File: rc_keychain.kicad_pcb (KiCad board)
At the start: 4 copper layers, 100 x 80 mm, 211 parts, among them J1 U.FL-R-SMT-1(10), J2 TYPE-C 16PIN 2MD(073), J3 Touch_Surface_Top, J4 Touch_Surface_Bottom, J5 5034801200, Q1 2N7002, SW1 TS35CA, U1 SF32LB525UC6, U10 LIS2DW12TR, U11 AP3602AKTR-G1, U12 SN74AUP1G17, U13 ST25R3916B-AQET, U2 MKDV1GCL-ABA, U3 TPS25200DRVT, U4 USBLC6-2P6, U5 USBLC6-2P6, U6 CAP1208-1-A4-TR, U7 CAP1208-1-A4-TR, U8 DRV2603RUNT, U9 TPS61040DBV, Y1 48MHz, Y2 32.768khz, Y3 27.12MHz

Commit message: fixups before manufacturing pt1
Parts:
- U10: value LIS2DW12TR -> LIS3DH; footprint LIS2DW12TR:LGA-12_L2.0-W2.0-P0.50-BL -> Package_LGA:LGA-16_3x3mm_P0.5mm_LayoutBorder3x5y
- moved JP15 2.61 mm to (126.5, 80.8)
- moved JP14 2.59 mm to (126.5, 83.4)
- moved C33 1.04 mm to (129.4, 80.0)
- moved C34 0.76 mm to (132.0, 79.1), turned to 90 degrees
- moved C35 0.70 mm to (131.0, 79.1), turned to 90 degrees
- moved U10 0.60 mm to (131.7, 82.0)
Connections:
- U10 pad 1: Net-(JP14-B) -> /interface/ACC_3V3_IN
- U10 pad 10: /interface/ACC_3V3_IN -> GND
- U10 pad 11: unconnected-(U10-INT2-Pad11) -> Net-(JP17-A)
- U10 pad 12: Net-(JP17-A) -> GND
- U10 pad 5: unconnected-(U10-NC-Pad5) -> GND
- U10 pad 6: GND -> Net-(JP14-B)
- U10 pad 7: GND -> unconnected-(U10-SDO-Pad7)
- U10 pad 8: GND -> /interface/ACC_3V3_IN
- U10 pad 9: /interface/ACC_3V3_IN -> unconnected-(U10-INT2-Pad9)
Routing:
- net Net-(JP17-A): track 5.57 -> 11.6 mm
- net /interface/ACC_3V3_IN: track 6.16 -> 8.99 mm
- net Net-(JP15-B): track 5.41 -> 4.00 mm
- net SDA: track 83.8 -> 85.0 mm
- net SCL: track 80.7 -> 81.8 mm
- net GND: track 110.8 -> 110.9 mm, vias 120 -> 123
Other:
- outline, holes or cut-outs redrawn

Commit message: fixups before manufacturing pt2
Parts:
- removed R1: 7.5k, Resistor_SMD:R_0603_1608Metric
- TP18: value SD_CLK -> FLASH_CLK
- TP19: value SD_CLK -> FLASH_CS
- TP20: value SD_DAT0 -> FLASH_DIO0
- TP21: value SD_DAT1 -> FLASH_DIO1
- TP22: value SD_DAT2 -> FLASH_DIO2
- TP23: value SD_DAT3 -> FLASH_DIO3
- U2: value MKDV1GCL-ABA -> GD25Q256EWIGR; footprint MKDV1GCL-ABA:LGA-8_L6.0-W8.0-P1.27-TL -> GD25Q256EWIGR:WSON-8_L6.0-W5.0-P1.27-TL-EP
- moved TP19 13.2 mm to (119.6, 111.8)
- moved TP23 12.0 mm to (129.8, 113.0)
- moved TP21 9.92 mm to (122.4, 109.6)
- moved TP22 8.06 mm to (124.5, 109.5)
- moved TP18 5.64 mm to (126.7, 109.6)
- moved TP20 2.06 mm to (130.5, 115.1)
- moved C5 1.45 mm to (128.9, 111.1)
- moved TP26 1.21 mm to (130.1, 108.9)
- moved U2 0.33 mm to (124.8, 113.4)
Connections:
- TP18 pad 1: SD_CLK -> FLASH_CLK
- TP19 pad 1: SD_CMD -> FLASH_CS
- TP20 pad 1: SD_DAT0 -> FLASH_DIO0
- TP21 pad 1: SD_DAT1 -> FLASH_DIO1
- TP22 pad 1: SD_DAT2 -> FLASH_DIO2
- TP23 pad 1: SD_DAT3 -> FLASH_DIO3
- U1 pad 28: SD_DAT1 -> FLASH_DIO3
- U1 pad 29: SD_DAT0 -> FLASH_CLK
- U1 pad 30: SD_CMD -> FLASH_DIO0
- U1 pad 31: SD_CLK -> FLASH_DIO2
- U1 pad 32: SD_DAT3 -> FLASH_DIO1
- U1 pad 33: SD_DAT2 -> FLASH_CS
- U2 pad 1: SD_DAT2 -> FLASH_CS
- U2 pad 2: SD_DAT3 -> FLASH_DIO1
- U2 pad 3: SD_CLK -> FLASH_DIO2
- U2 pad 5: SD_CMD -> FLASH_DIO0
- U2 pad 6: SD_DAT0 -> FLASH_CLK
- U2 pad 7: SD_DAT1 -> FLASH_DIO3
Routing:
- net SD_DAT3: track 22.0 -> 0.00 mm
- net SD_DAT1: track 20.3 -> 0.00 mm, vias 2 -> 0
- net FLASH_CLK: track 0.00 -> 18.0 mm
- net SD_DAT0: track 17.7 -> 0.00 mm, vias 2 -> 0
- net FLASH_DIO3: track 0.00 -> 16.5 mm
- net SD_CLK: track 16.2 -> 0.00 mm
- net FLASH_DIO0: track 0.00 -> 15.8 mm, vias 0 -> 2
- net SD_CMD: track 15.2 -> 0.00 mm
- net FLASH_DIO2: track 0.00 -> 14.8 mm
- net FLASH_CS: track 0.00 -> 14.1 mm
- net SD_DAT2: track 13.9 -> 0.00 mm
- net FLASH_DIO1: track 0.00 -> 13.8 mm
- net +3V3_G1: track 14.0 -> 12.4 mm, vias 4 -> 3
- net GND: track 110.9 -> 110.7 mm, vias 123 -> 124

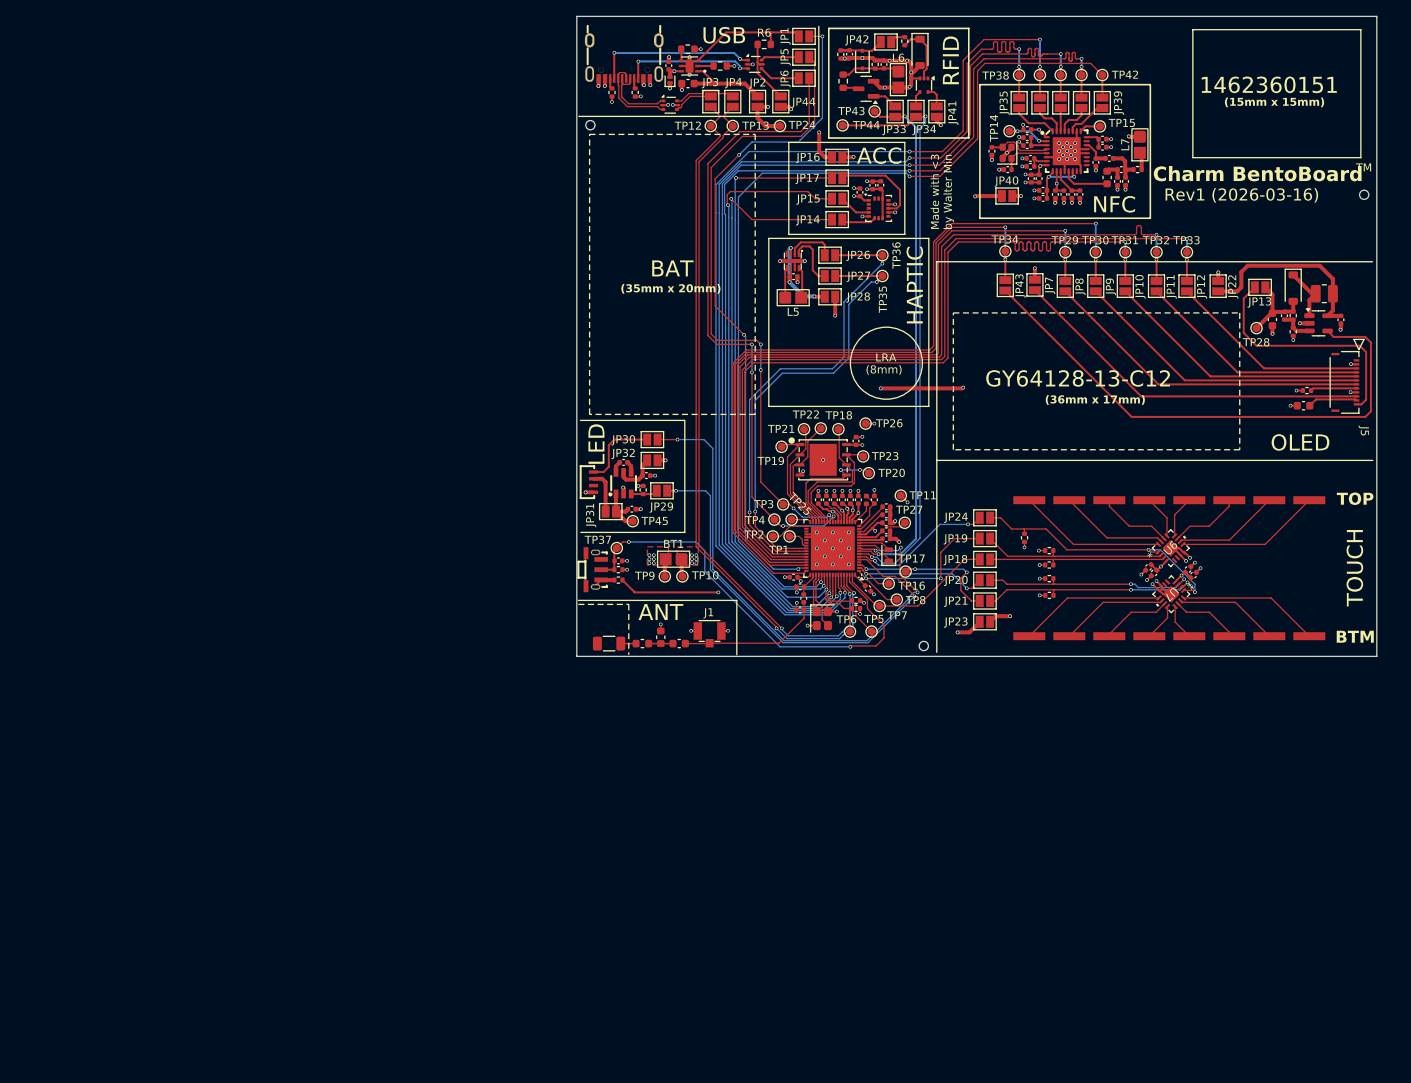
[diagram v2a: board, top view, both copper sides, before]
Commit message: revise some decoupling caps to be 0201
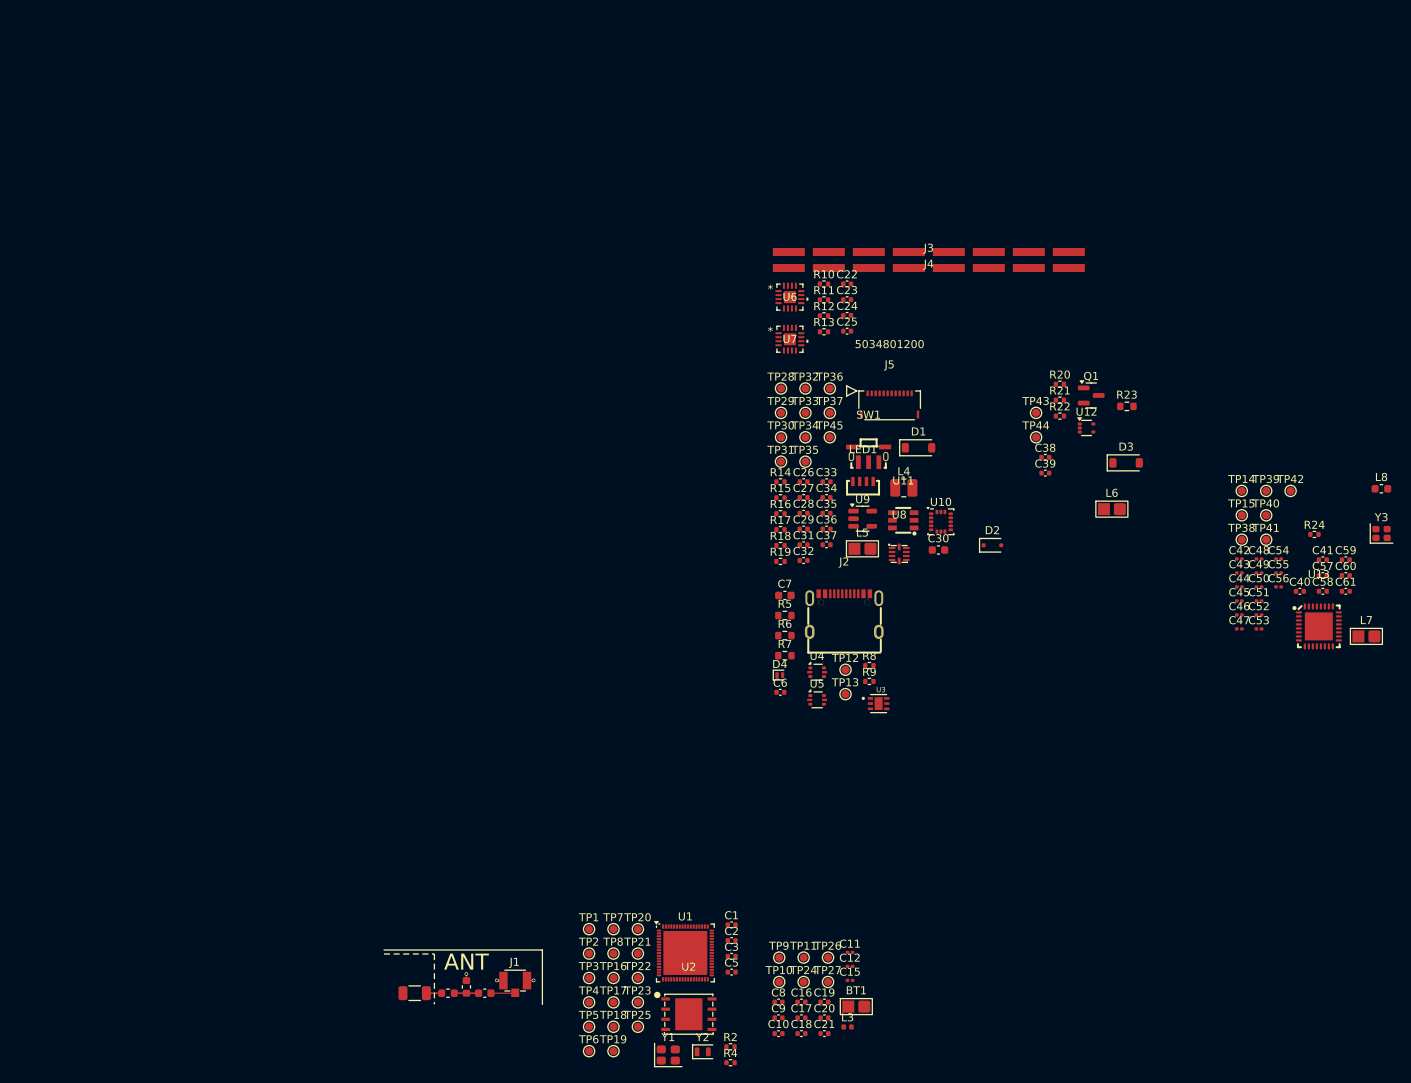
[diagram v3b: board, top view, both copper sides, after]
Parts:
- removed C13, C14: 4.7uF, Capacitor_SMD:C_0402_1005Metric
- removed JP1: USB_OVP_FAULT, Jumper:SolderJumper-2_P1.3mm_Open_Pad1.0x1.5mm
- removed JP10: OLED_DC, Jumper:SolderJumper-2_P1.3mm_Open_Pad1.0x1.5mm
- removed JP11: OLED_CLK, Jumper:SolderJumper-2_P1.3mm_Open_Pad1.0x1.5mm
- removed JP12: OLED_DAT, Jumper:SolderJumper-2_P1.3mm_Open_Pad1.0x1.5mm
- removed JP13: OLED_9V, Jumper:SolderJumper-2_P1.3mm_Open_Pad1.0x1.5mm
- removed JP14: ACC_SCL, Jumper:SolderJumper-2_P1.3mm_Open_Pad1.0x1.5mm
- removed JP15: ACC_SDA, Jumper:SolderJumper-2_P1.3mm_Open_Pad1.0x1.5mm
- removed JP16: ACC_3V3, Jumper:SolderJumper-2_P1.3mm_Open_Pad1.0x1.5mm
- removed JP17: ACC_INT, Jumper:SolderJumper-2_P1.3mm_Open_Pad1.0x1.5mm
- removed JP18: TOUCH_SCL_T1, Jumper:SolderJumper-2_P1.3mm_Open_Pad1.0x1.5mm
- removed JP19: TOUCH_SDA_T1, Jumper:SolderJumper-2_P1.3mm_Open_Pad1.0x1.5mm
- removed JP2: USB_VBUS, Jumper:SolderJumper-2_P1.3mm_Open_Pad1.0x1.5mm
- removed JP20: TOUCH_SCL_T2, Jumper:SolderJumper-2_P1.3mm_Open_Pad1.0x1.5mm
- removed JP21: TOUCH_SDA_T2, Jumper:SolderJumper-2_P1.3mm_Open_Pad1.0x1.5mm
- removed JP22: OLED_VBAT, Jumper:SolderJumper-2_P1.3mm_Open_Pad1.0x1.5mm
- removed JP23: TOUCH_3V3_G2, Jumper:SolderJumper-2_P1.3mm_Open_Pad1.0x1.5mm
- removed JP24: TOUCH_INT, Jumper:SolderJumper-2_P1.3mm_Open_Pad1.0x1.5mm
- removed JP26: HAPTIC_PWM, Jumper:SolderJumper-2_P1.3mm_Open_Pad1.0x1.5mm
- removed JP27: HAPTIC_EN, Jumper:SolderJumper-2_P1.3mm_Open_Pad1.0x1.5mm
- removed JP28: HAPTIC_VBAT, Jumper:SolderJumper-2_P1.3mm_Open_Pad1.0x1.5mm
- removed JP29: LED_EN, Jumper:SolderJumper-2_P1.3mm_Open_Pad1.0x1.5mm
- removed JP3: USB_DP, Jumper:SolderJumper-2_P1.3mm_Open_Pad1.0x1.5mm
- removed JP30: LED_DAT, Jumper:SolderJumper-2_P1.3mm_Open_Pad1.0x1.5mm
- removed JP31: LED_5V, Jumper:SolderJumper-2_P1.3mm_Open_Pad1.0x1.5mm
- removed JP32: LED_VBAT, Jumper:SolderJumper-2_P1.3mm_Open_Pad1.0x1.5mm
- removed JP33: RFID_DAT, Jumper:SolderJumper-2_P1.3mm_Open_Pad1.0x1.5mm
- removed JP34: RFID_WAKE, Jumper:SolderJumper-2_P1.3mm_Open_Pad1.0x1.5mm
- removed JP35: NFC_DI, Jumper:SolderJumper-2_P1.3mm_Open_Pad1.0x1.5mm
- removed JP36: NFC_DO, Jumper:SolderJumper-2_P1.3mm_Open_Pad1.0x1.5mm
- removed JP37: NFC_CLK, Jumper:SolderJumper-2_P1.3mm_Open_Pad1.0x1.5mm
- removed JP38: NFC_CS, Jumper:SolderJumper-2_P1.3mm_Open_Pad1.0x1.5mm
- removed JP39: NFC_INT, Jumper:SolderJumper-2_P1.3mm_Open_Pad1.0x1.5mm
- removed JP4: USB_DN, Jumper:SolderJumper-2_P1.3mm_Open_Pad1.0x1.5mm
- removed JP40: NFC_3V3, Jumper:SolderJumper-2_P1.3mm_Open_Pad1.0x1.5mm
- removed JP41: RFID_3V3, Jumper:SolderJumper-2_P1.3mm_Open_Pad1.0x1.5mm
- removed JP42: RFID_WAKE_RAW, Jumper:SolderJumper-2_P1.3mm_Open_Pad1.0x1.5mm
- removed JP43: OLED_EN, Jumper:SolderJumper-2_P1.3mm_Open_Pad1.0x1.5mm
- removed JP44: USB_3V3, Jumper:SolderJumper-2_P1.3mm_Open_Pad1.0x1.5mm
- removed JP5: USB_DBG_A, Jumper:SolderJumper-2_P1.3mm_Open_Pad1.0x1.5mm
- removed JP6: USB_DBG_B, Jumper:SolderJumper-2_P1.3mm_Open_Pad1.0x1.5mm
- removed JP7: OLED_3V3_G2, Jumper:SolderJumper-2_P1.3mm_Open_Pad1.0x1.5mm
- removed JP8: OLED_CS, Jumper:SolderJumper-2_P1.3mm_Open_Pad1.0x1.5mm
- removed JP9: OLED_RST, Jumper:SolderJumper-2_P1.3mm_Open_Pad1.0x1.5mm
- removed R3: 100k, Resistor_SMD:R_0402_1005Metric
- C11, C12, C15, C42, C43, C44, C45, C46, C47, C48, C49, C50, C51, C52, C53, C54, C55, C56: footprint Capacitor_SMD:C_0402_1005Metric -> Capacitor_SMD:C_0201_0603Metric
- C28: footprint Capacitor_SMD:C_0603_1608Metric -> Capacitor_SMD:C_0402_1005Metric
- moved TP24 107.0 mm to (122.4, 178.7)
- moved U3 83.1 mm to (131.7, 143.9), turned to 0 degrees
- moved R9 80.3 mm to (130.6, 141.1), turned to 0 degrees
- moved U5 79.8 mm to (124.0, 143.4)
- moved TP18 79.8 mm to (98.6, 184.3)
- moved C6 79.6 mm to (119.4, 142.5), turned to 0 degrees
- moved TP19 78.4 mm to (98.6, 187.3)
- moved R8 77.4 mm to (130.6, 139.1), turned to 0 degrees
- moved D4 75.6 mm to (119.4, 140.3), turned to 0 degrees
- moved J2 74.4 mm to (127.4, 132.6), turned to 0 degrees
- moved R7 74.2 mm to (120.0, 137.9)
- moved R6 73.9 mm to (120.0, 135.4)
- moved TP23 73.8 mm to (101.6, 181.2)
- moved U4 73.2 mm to (124.0, 140.0)
- moved TP13 72.4 mm to (127.6, 142.7)
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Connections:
- C22 pad 1: /touch/+3V3_G2_IN -> +3V3_G2
- C23 pad 1: /touch/+3V3_G2_IN -> +3V3_G2
- C24 pad 1: /touch/+3V3_G2_IN -> +3V3_G2
- C25 pad 1: /touch/+3V3_G2_IN -> +3V3_G2
- C26 pad 1: /interface/HAPTIC_VBAT_IN -> VBAT
- C27 pad 1: Net-(JP22-B) -> VBAT
- C29 pad 1: Net-(D1-A) -> +9V
- C30 pad 1: Net-(D1-A) -> +9V
- C32 pad 1: Net-(JP32-B) -> VBAT
- C33 pad 1: /interface/ACC_3V3_IN -> +3V3
- C34 pad 1: /interface/ACC_3V3_IN -> +3V3
- C35 pad 1: /interface/ACC_3V3_IN -> +3V3
- C37 pad 1: Net-(JP31-A) -> +5V
- C38 pad 1: Net-(D2-K) -> Net-(D2-A)
- C39 pad 2: Net-(D2-A) -> Net-(D2-K)
- C44 pad 1: /rf/NFC_3V3_IN -> +3V3
- C51 pad 1: /rf/NFC_3V3_IN -> +3V3
- C52 pad 1: /rf/NFC_3V3_IN -> +3V3
- C53 pad 1: /rf/NFC_3V3_IN -> +3V3
- C54 pad 1: /rf/NFC_3V3_IN -> +3V3
- C7 pad 1: Net-(JP2-A) -> VBUS
- D1 pad 1: Net-(D1-K) -> +9V
- D4 pad 1: GND -> /usb/VBUS_RAW
- D4 pad 2: /usb/VBUS_RAW -> GND
- J5 pad 10: /interface/+3V3_G2_IN -> +3V3_G2
- J5 pad 3: /interface/OLED_DAT_IN -> OLED_DAT
- J5 pad 4: /interface/OLED_CLK_IN -> OLED_CLK
- J5 pad 5: /interface/OLED_DC_IN -> OLED_DC
- J5 pad 6: /interface/OLED_RST_IN -> OLED_RST
- J5 pad 7: /interface/OLED_CS_IN -> OLED_CS
- L4 pad 1: Net-(JP22-B) -> VBAT
- L4 pad 2: Net-(D1-K) -> Net-(D1-A)
- L6 pad 2: Net-(D2-K) -> Net-(D2-A)
- LED1 pad 4: /interface/LED_DAT_IN -> LED_DAT
- Q1 pad 1: /rf/RFID_DAT_IN -> RFID_DAT
- R10 pad 1: /touch/+3V3_G2_IN -> +3V3_G2
- R10 pad 2: Net-(JP19-B) -> SDA_T1
- R11 pad 1: /touch/+3V3_G2_IN -> +3V3_G2
- R11 pad 2: Net-(JP21-B) -> SDA_T2
- R12 pad 1: /touch/+3V3_G2_IN -> +3V3_G2
- R12 pad 2: Net-(JP18-B) -> SCL_T1
- R13 pad 1: /touch/+3V3_G2_IN -> +3V3_G2
- R13 pad 2: Net-(JP20-B) -> SCL_T2
- R16 pad 1: Net-(D1-A) -> +9V
- R19 pad 1: /interface/LED_EN_IN -> LED_EN
- R20 pad 1: Net-(D2-K) -> Net-(D2-A)
- R21 pad 1: Net-(JP42-B) -> Net-(D2-K)
- R22 pad 1: Net-(D2-A) -> Net-(D2-K)
- R23 pad 1: Net-(D2-K) -> Net-(D2-A)
- R6 pad 1: /usb/USB_3V3_IN -> +3V3
- R6 pad 2: Net-(JP1-A) -> OVP_FAULT
- TP28 pad 1: Net-(D1-A) -> +9V
- TP45 pad 1: Net-(JP31-A) -> +5V
- U10 pad 1: /interface/ACC_3V3_IN -> +3V3
- U10 pad 11: Net-(JP17-A) -> ACC_INT
- U10 pad 14: /interface/ACC_3V3_IN -> +3V3
- U10 pad 4: Net-(JP15-B) -> SCL
- U10 pad 6: Net-(JP14-B) -> SDA
- U10 pad 7: unconnected-(U10-SDO-Pad7) -> GND
- U11 pad 1: Net-(JP31-A) -> +5V
- U11 pad 3: /interface/LED_EN_IN -> LED_EN
- U11 pad 5: Net-(JP32-B) -> VBAT
- U12 pad 4: /rf/RFID_WAKE_IN -> RFID_WAKE
- U12 pad 5: /rf/RFID_3V3_IN -> +3V3
- U13 pad 1: /rf/NFC_3V3_IN -> +3V3
- U13 pad 10: /rf/NFC_3V3_IN -> +3V3
- U13 pad 27: /rf/NFC_INT_IN -> NFC_INT
- U13 pad 29: /rf/NFC_CS_IN -> NFC_CS
- U13 pad 30: /rf/NFC_CLK_IN -> NFC_CLK
- U13 pad 31: /rf/NFC_DO_IN -> NFC_DO
- U13 pad 32: /rf/NFC_DI_IN -> NFC_DI
- U13 pad 8: /rf/NFC_3V3_IN -> +3V3
- U3 pad 1: Net-(JP2-A) -> VBUS
- U3 pad 3: Net-(JP1-A) -> OVP_FAULT
- U4 pad 4: /usb/USB_PROT_DP -> USB_DP
- U4 pad 6: /usb/USB_PROT_DN -> USB_DN
- U5 pad 4: Net-(JP6-A) -> DBG_B
- U5 pad 6: Net-(JP5-A) -> DBG_A
- U6 pad 1: /touch/TOUCH_INT_IN -> TOUCH_INT
- U6 pad 2: Net-(JP19-B) -> SDA_T1
- U6 pad 3: Net-(JP18-B) -> SCL_T1
- U6 pad 4: /touch/+3V3_G2_IN -> +3V3_G2
- U7 pad 1: /touch/TOUCH_INT_IN -> TOUCH_INT
- U7 pad 2: Net-(JP21-B) -> SDA_T2
- U7 pad 3: Net-(JP20-B) -> SCL_T2
- U7 pad 4: /touch/+3V3_G2_IN -> +3V3_G2
- U8 pad 1: Net-(JP27-B) -> HAPTIC_EN
- U8 pad 2: Net-(JP26-B) -> HAPTIC_PWM
- U8 pad 3: /interface/HAPTIC_VBAT_IN -> VBAT
- U8 pad 7: /interface/HAPTIC_VBAT_IN -> VBAT
- U9 pad 1: Net-(D1-K) -> Net-(D1-A)
- U9 pad 4: /interface/OLED_EN_IN -> OLED_EN
- U9 pad 5: Net-(JP22-B) -> VBAT
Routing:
- net NFC_DO: track 129.2 -> 0.00 mm, vias 4 -> 0
- net NFC_CS: track 129.2 -> 0.00 mm, vias 4 -> 0
- net NFC_CLK: track 129.2 -> 0.00 mm, vias 4 -> 0
- net NFC_DI: track 129.1 -> 0.00 mm, vias 4 -> 0
- net NFC_INT: track 118.0 -> 0.00 mm, vias 2 -> 0
- net GND: track 110.7 -> 2.50 mm, vias 124 -> 3
- net OLED_DAT: track 105.5 -> 0.00 mm, vias 2 -> 0
- net OLED_CLK: track 105.5 -> 0.00 mm, vias 2 -> 0
- net OLED_DC: track 105.4 -> 0.00 mm, vias 2 -> 0
- net OLED_RST: track 100.9 -> 0.00 mm, vias 2 -> 0
- net OLED_CS: track 94.0 -> 0.00 mm, vias 2 -> 0
- net USB_DP: track 89.8 -> 0.00 mm, vias 2 -> 0
- net USB_DN: track 88.3 -> 0.00 mm, vias 2 -> 0
- net OLED_EN: track 87.8 -> 0.00 mm, vias 2 -> 0
- net SDA: track 85.0 -> 0.00 mm, vias 2 -> 0
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- added copper zone on In2.Cu, net (none)
- removed copper zone on In2.Cu, net /interface/HAPTIC_VBAT_IN
- removed copper zone on In2.Cu, net /rf/NFC_3V3_IN
- removed copper zone on In2.Cu, net /touch/+3V3_G2_IN
- removed copper zone on F.Cu, net GND
- removed copper zone on F.Cu, net VBAT
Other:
- board outline removed
- board text removed: "(15mm x 15mm)"
- board text removed: "(35mm x 20mm)"
- board text removed: "(36mm x 17mm)"
- board text removed: "(8mm)"
- board text removed: "1462360151"
- board text removed: "ACC"
- board text removed: "BAT"
- board text removed: "BTM"
- board text removed: "Charm BentoBoard"
- board text removed: "GY64128-13-C12"
- board text removed: "HAPTIC"
- board text removed: "LED"
- board text removed: "LRA"
- board text removed: "Made with <3 by Walter Min"
- board text removed: "NFC"
- board text removed: "OLED"
- board text removed: "RFID"
- board text removed: "Rev1 (2026-03-16)"
- board text removed: "TM"
- board text removed: "TOP"
- board text removed: "TOUCH"
- board text removed: "USB"

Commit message: layout progress
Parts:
- removed J1: U.FL-R-SMT-1(10), U.FL-R-SMT-1_10_:HRS_U.FL-R-SMT-1_10_
- removed TP18: FLASH_CLK, TestPoint:TestPoint_Pad_D1.0mm
- removed TP19: FLASH_CS, TestPoint:TestPoint_Pad_D1.0mm
- removed TP20: FLASH_DIO0, TestPoint:TestPoint_Pad_D1.0mm
- removed TP21: FLASH_DIO1, TestPoint:TestPoint_Pad_D1.0mm
- removed TP22: FLASH_DIO2, TestPoint:TestPoint_Pad_D1.0mm
- removed TP23: FLASH_DIO3, TestPoint:TestPoint_Pad_D1.0mm
- removed TP29: OLED_CS, TestPoint:TestPoint_Pad_D1.0mm
- removed TP30: OLED_RST, TestPoint:TestPoint_Pad_D1.0mm
- removed TP31: OLED_DC, TestPoint:TestPoint_Pad_D1.0mm
- removed TP32: OLED_CLK, TestPoint:TestPoint_Pad_D1.0mm
- removed TP33: OLED_DAT, TestPoint:TestPoint_Pad_D1.0mm
- removed TP34: OLED_EN, TestPoint:TestPoint_Pad_D1.0mm
- removed TP35: HAPTIC_EN, TestPoint:TestPoint_Pad_D1.0mm
- removed TP36: HAPTIC_PWM, TestPoint:TestPoint_Pad_D1.0mm
- removed TP38: NFC_DI, TestPoint:TestPoint_Pad_D1.0mm
- removed TP39: NFC_DO, TestPoint:TestPoint_Pad_D1.0mm
- removed TP40: NFC_CLK, TestPoint:TestPoint_Pad_D1.0mm
- removed TP41: NFC_CS, TestPoint:TestPoint_Pad_D1.0mm
- removed TP42: NFC_INT, TestPoint:TestPoint_Pad_D1.0mm
- removed TP43: RFID_DAT, TestPoint:TestPoint_Pad_D1.0mm
- removed TP44: RFID_WAKE, TestPoint:TestPoint_Pad_D1.0mm
- added C13: 4.7uF, Capacitor_SMD:C_0201_0603Metric, F.Cu at (62.5, 119.3)
- added C14: 4.7uF, Capacitor_SMD:C_0201_0603Metric, F.Cu at (61.7, 119.3)
- C10, C19: footprint Capacitor_SMD:C_0402_1005Metric -> Capacitor_SMD:C_0201_0603Metric
- moved SW1 103.9 mm to (26.7, 107.5)
- moved C10 94.4 mm to (53.9, 117.0), turned to 180 degrees
- moved Y1 92.1 mm to (52.9, 112.2), turned to -90 degrees
- moved L3 90.8 mm to (63.8, 120.0), turned to -90 degrees
- moved C20 90.7 mm to (64.5, 115.6)
- moved C15 90.3 mm to (59.9, 119.3), turned to -90 degrees
- moved C12 89.8 mm to (59.1, 119.3), turned to -90 degrees
- moved C21 88.7 mm to (64.8, 120.0), turned to 90 degrees
- moved C9 88.4 mm to (64.5, 113.8)
- moved C18 88.0 mm to (64.5, 118.6)
- moved C11 87.8 mm to (64.3, 114.7)
- moved C17 87.3 mm to (64.5, 117.6)
- moved C16 87.0 mm to (60.8, 119.5), turned to -90 degrees
- moved Y2 85.4 mm to (57.1, 120.2)
- moved J2 85.2 mm to (43.8, 116.5), turned to -90 degrees
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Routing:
- net FLASH_DIO3: track 0.00 -> 12.5 mm
- net FLASH_CLK: track 0.00 -> 10.7 mm
- net FLASH_DIO0: track 0.00 -> 8.00 mm
- net Net-(U1A-BUCK_FB): track 0.00 -> 5.13 mm
- net VBAT: track 19.5 -> 24.5 mm, vias 0 -> 2
- net GND: track 2.50 -> 7.38 mm, vias 3 -> 14
- net FLASH_CS: track 0.00 -> 4.84 mm
- net Net-(U1B-PA23): track 0.00 -> 4.34 mm
- net FLASH_DIO1: track 0.00 -> 4.04 mm
- net Net-(U1B-PA22): track 0.00 -> 3.67 mm
- net +3V3_G1: track 6.51 -> 9.86 mm, vias 0 -> 1
- net Net-(U1A-BUCK_LX): track 0.00 -> 3.23 mm
- net Net-(C2-Pad2): track 3.05 -> 0.00 mm
- net +3V3: track 7.91 -> 10.9 mm, vias 0 -> 1
- net FLASH_DIO2: track 0.00 -> 2.66 mm
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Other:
- board outline added: 58 x 18 mm
- board text removed: "ANT"

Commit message: progress
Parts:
- removed C1, C3: NF, Capacitor_SMD:C_0402_1005Metric
- added REF**: Touch_Surface_8_Pad_Slim, custom_footprints:Touch_Surface_8_Pad_Slim, B.Cu at (78.5, 104.2)
- added REF**: Touch_Surface_8_Pad_Slim, custom_footprints:Touch_Surface_8_Pad_Slim, B.Cu at (78.5, 121.8)
- AE1, C10, C11, C12, C13, C14, C15, C16, C17, C18, C2, C20, C21, C4, C5, C8, C9, J2, J5, L1, L2, L3, U1, U2, U4, U5, Y2: moved to B.Cu
- J3, J4: footprint custom_footprints:Touch_Surface_8_Pad -> custom_footprints:Touch_Surface_8_Pad_Slim
- Y1: footprint Crystal:Crystal_SMD_2520-4Pin_2.5x2.0mm -> Crystal:Crystal_SMD_2016-4Pin_2.0x1.6mm; moved to B.Cu
- moved R24 100.1 mm to (92.2, 88.5)
- moved C40 100.1 mm to (90.4, 95.6)
- moved C41 100.1 mm to (93.3, 91.6)
- moved C48 100.1 mm to (85.3, 91.5)
- moved C49 100.1 mm to (85.3, 93.3)
- moved C50 100.1 mm to (85.3, 95.0)
- moved C51 100.1 mm to (85.3, 96.8)
- moved C52 100.1 mm to (85.3, 98.5)
- moved C53 100.1 mm to (85.3, 100.3)
- moved C54 100.1 mm to (87.7, 91.5)
- moved C55 100.1 mm to (87.7, 93.3)
- moved C56 100.1 mm to (87.7, 95.0)
- moved C57 100.1 mm to (93.3, 93.6)
- moved C58 100.1 mm to (93.3, 95.6)
- moved C59 100.1 mm to (96.1, 91.6)
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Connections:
- C32 pad 1: VBAT -> +3V3_G2
- R10 pad 2: SDA_T1 -> SDA_T2
- R11 pad 2: SDA_T2 -> SDA_T1
- R12 pad 2: SCL_T1 -> SCL_T2
- R13 pad 2: SCL_T2 -> SCL_T1
- U10 pad 8: /interface/ACC_3V3_IN -> +3V3
- U11 pad 5: VBAT -> +3V3_G2
- U6 pad 2: SDA_T1 -> SDA_T2
- U6 pad 3: SCL_T1 -> SCL_T2
- U7 pad 10: Net-(J4-Pin_2) -> Net-(J4-Pin_7)
- U7 pad 11: Net-(J4-Pin_3) -> Net-(J4-Pin_6)
- U7 pad 12: Net-(J4-Pin_4) -> Net-(J4-Pin_5)
- U7 pad 13: Net-(J4-Pin_5) -> Net-(J4-Pin_4)
- U7 pad 14: Net-(J4-Pin_6) -> Net-(J4-Pin_3)
- U7 pad 15: Net-(J4-Pin_7) -> Net-(J4-Pin_2)
- U7 pad 16: Net-(J4-Pin_8) -> Net-(J4-Pin_1)
- U7 pad 2: SDA_T2 -> SDA_T1
- U7 pad 3: SCL_T2 -> SCL_T1
- U7 pad 9: Net-(J4-Pin_1) -> Net-(J4-Pin_8)
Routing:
- net TOUCH_INT: track 2.41 -> 0.00 mm
- net SDA_T1: track 1.84 -> 0.00 mm, vias 1 -> 0
- net SDA_T2: track 2.55 -> 3.95 mm, vias 1 -> 0
- net Net-(C2-Pad2): track 0.00 -> 1.26 mm
- net GND: track 7.38 -> 8.14 mm, vias 14 -> 18
- net SCL_T2: track 2.60 -> 3.18 mm, vias 1 -> 0
- net +3V3_G2: vias 1 -> 3
- net (no net): vias 0 -> 2
- added copper zone on In2.Cu, net GND
- removed copper zone on In2.Cu, net /interface/ACC_3V3_IN
